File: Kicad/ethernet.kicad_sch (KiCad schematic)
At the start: 27 parts, among them J14001 RJ45 MagJack, U14001 ENC424J600, Y14001 25M

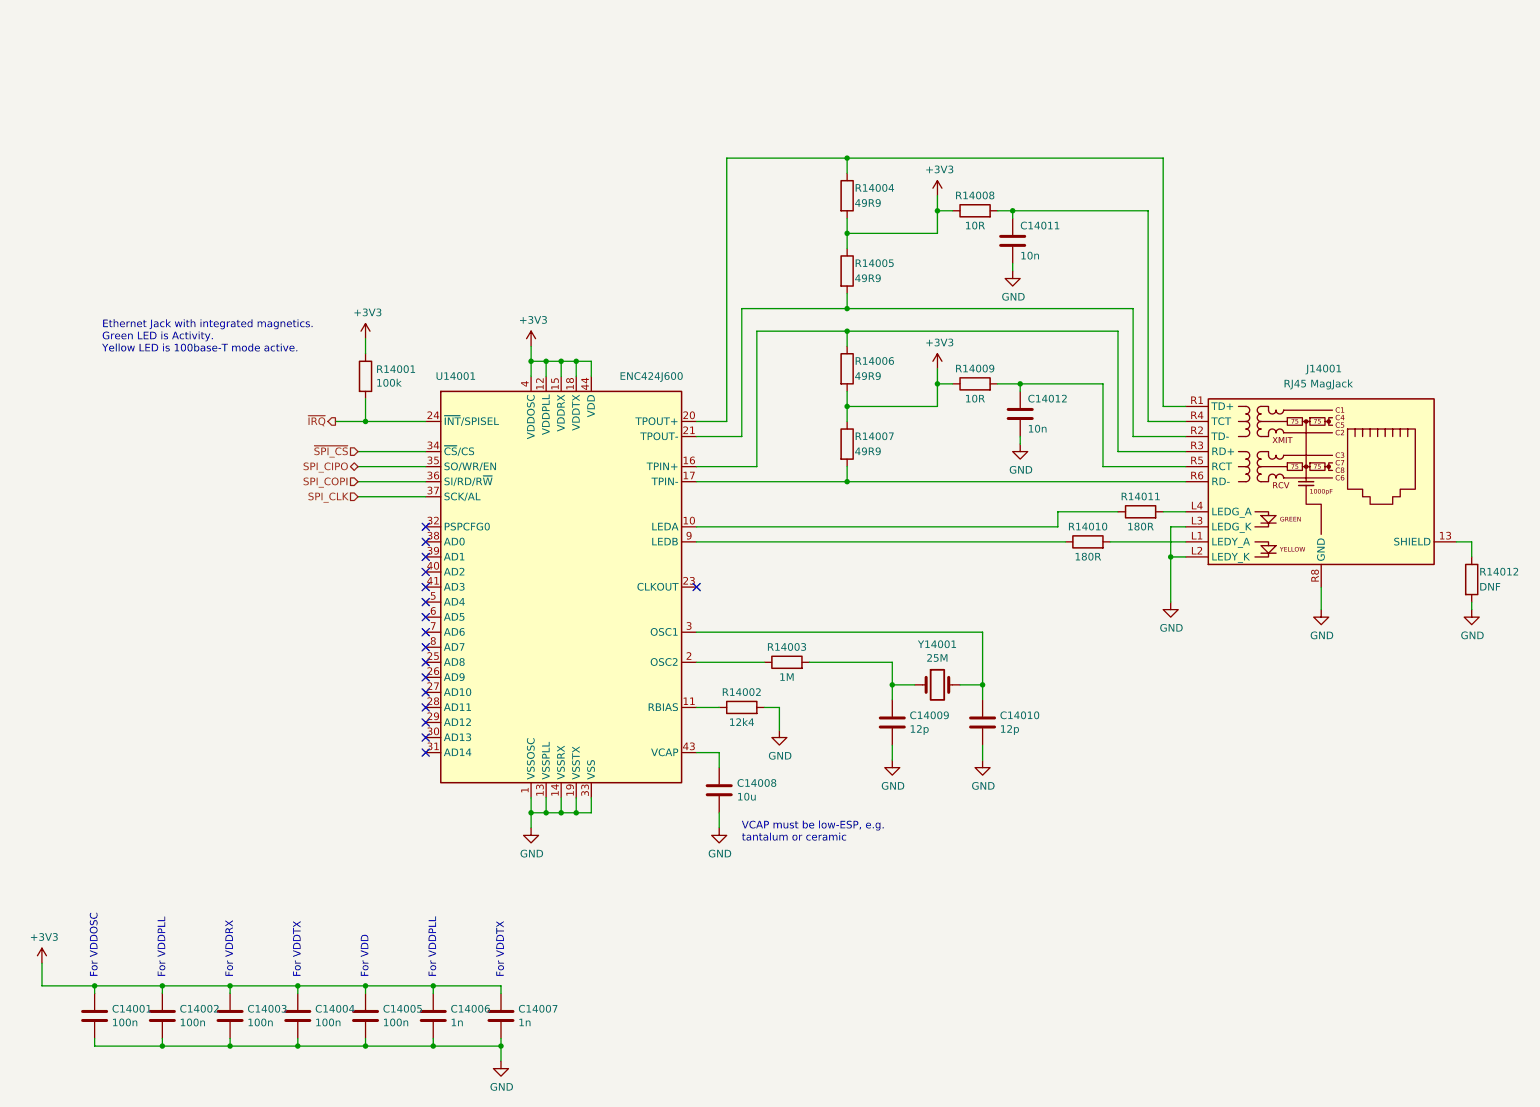
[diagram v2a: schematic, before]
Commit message: Re-imported from Neotron Pico v1.1.
This time I deleted the sheets from the top level and then re-added pointing at the new files. I also reset the PCB dimensions to match the Neotron Pico.

This seems to have done a better job importing footprints.
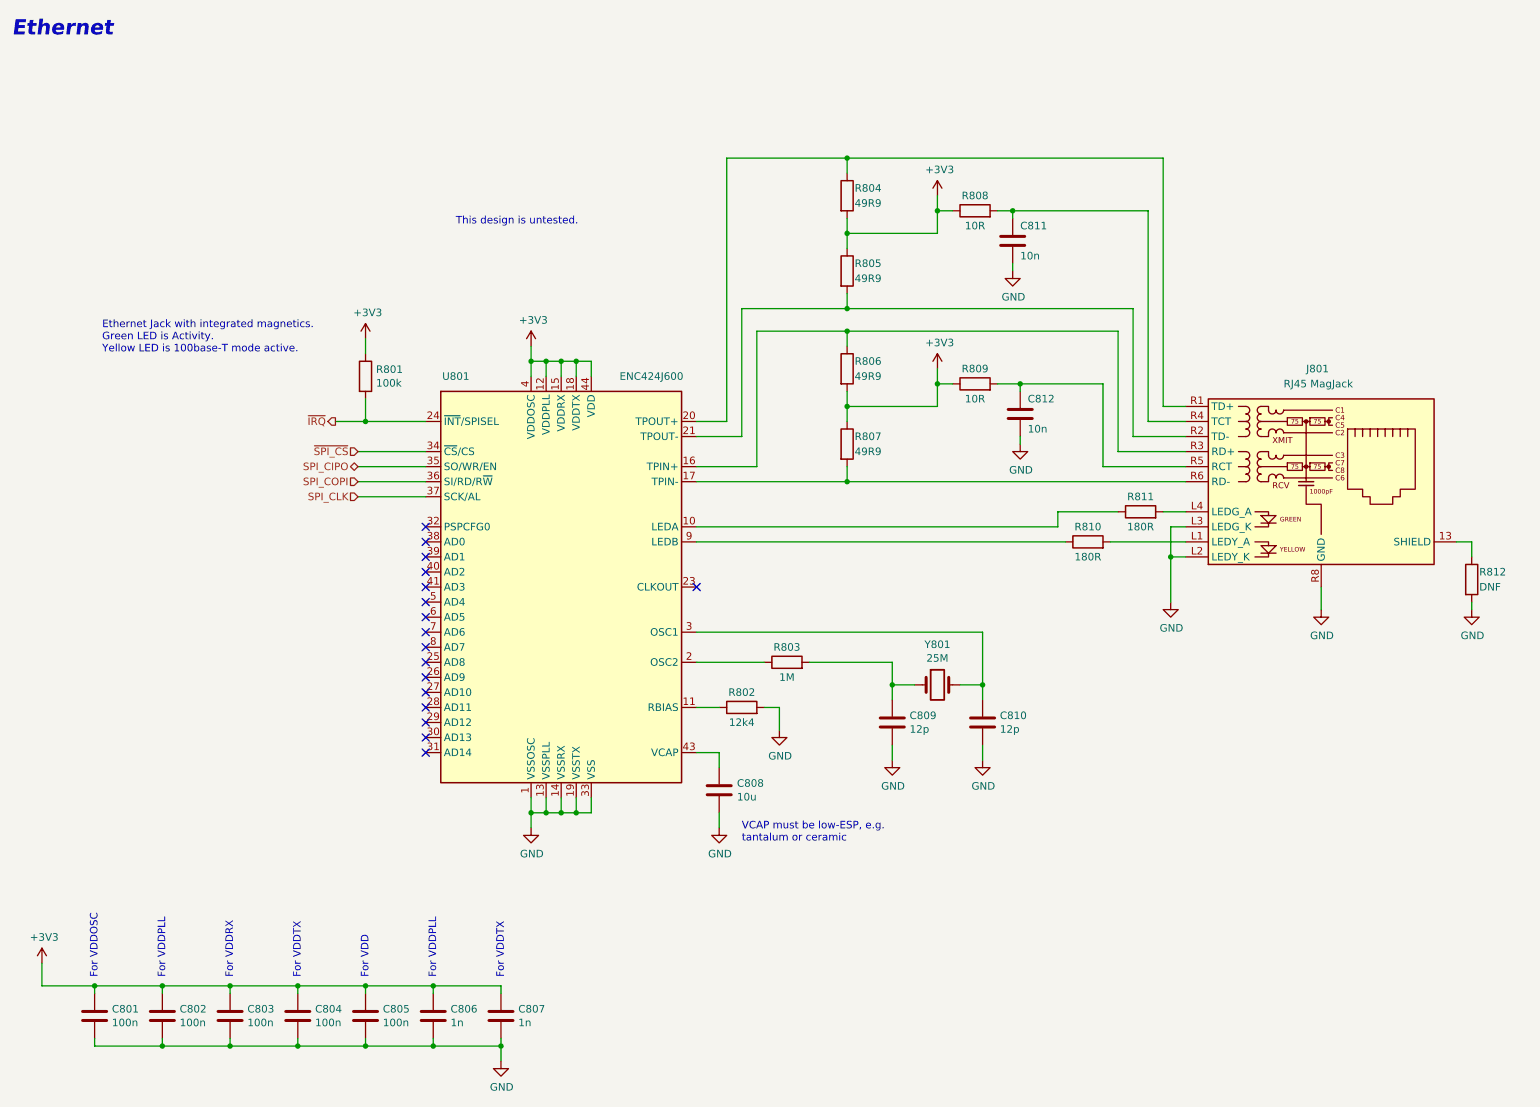
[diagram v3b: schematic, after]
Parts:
- renumbered C14001 to C801, C14002 to C802, C14003 to C803, C14004 to C804, C14005 to C805, C14006 to C806, C14007 to C807, C14008 to C808, C14009 to C809, C14010 to C810, C14011 to C811, C14012 to C812, J14001 to J801, R14001 to R801, R14002 to R802, R14003 to R803, R14004 to R804, R14005 to R805, R14006 to R806, R14007 to R807, R14008 to R808, R14009 to R809, R14010 to R810, R14011 to R811, R14012 to R812, U14001 to U801, Y14001 to Y801
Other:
- note added: "Ethernet"
- note added: "This design is untested."
